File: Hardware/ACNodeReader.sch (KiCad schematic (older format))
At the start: 34 parts, among them J1 Conn_01x08_Male, J2 AVR-ISP-6, J3 Conn_01x04_Female, J4 Conn_01x02_Male, J5 Conn_01x04_Female, J6 Conn_01x04_Male, J7 Conn_01x04_Male, U1 L78L05_SOT89, U2 ATmega88PB-AU, U3 ISL8489EIBZ, U4 LM75C, Y1 Crystal_GND24

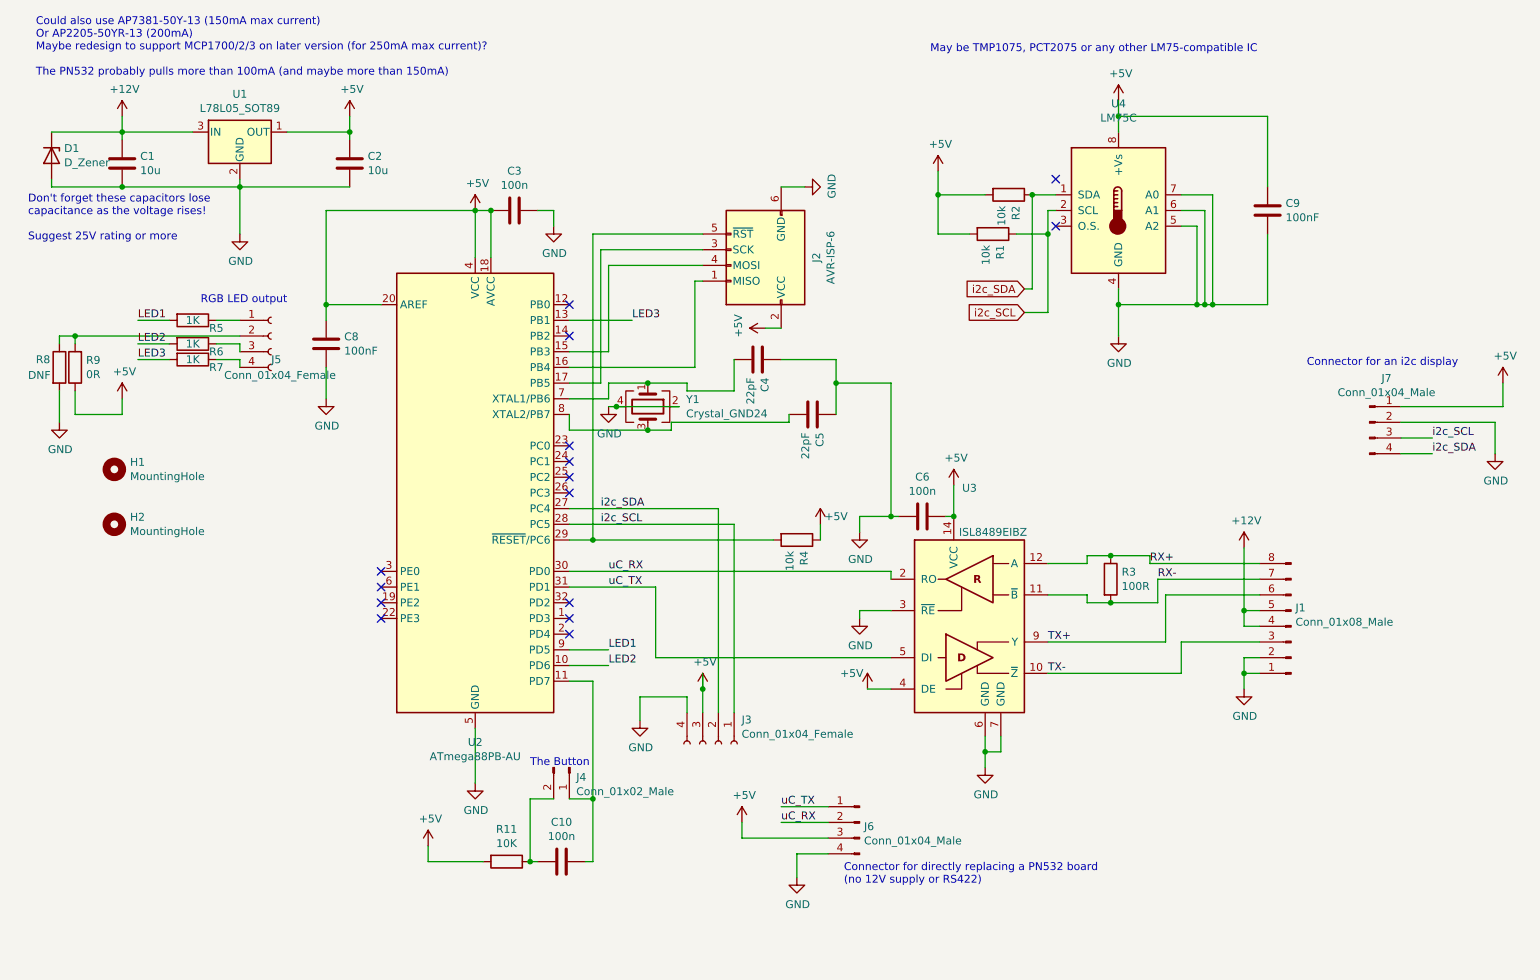
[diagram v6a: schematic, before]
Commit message: Hardware V1.1 - 3.3V with chunkier 5V regulator
The 1.0 5V regulator wasn't chunky enough, so this board has a larger
one to support the current draw of the PN532 module. Additionally, a
capacitor has been added near to the PN532 module connector to assist in
smoothing the supply to it.

Most of the board now runs at 3.3V, derived from the 5V rail. This is to
support direct connection to an ACNode, which only support 3.3V IO. This
required slowing the AVR down to 12MHz. An alternative option would have
been to use a level shifter on the TX line.
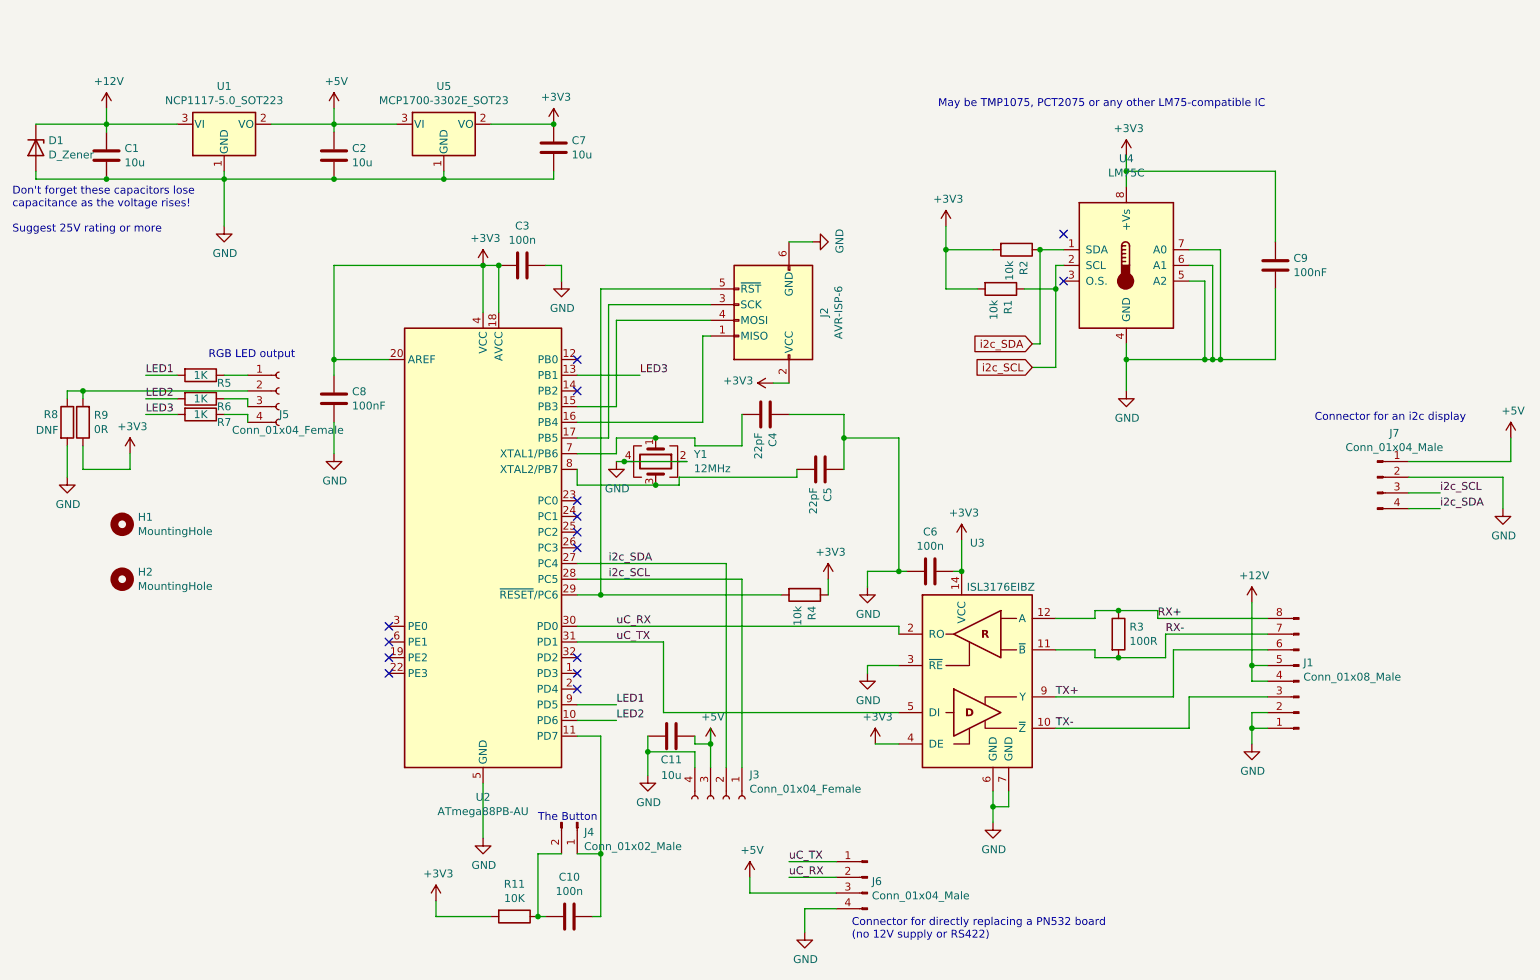
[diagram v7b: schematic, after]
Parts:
- removed U1: L78L05_SOT89, Package_TO_SOT_SMD:SOT-89-3, symbol Regulator_Linear:L78L05_SOT89
- added C11, C7: 10u, Capacitor_SMD:C_0805_2012Metric, symbol Device:C
- added U1: NCP1117-5.0_SOT223, Package_TO_SOT_SMD:SOT-223-3_TabPin2, symbol Regulator_Linear:NCP1117-5.0_SOT223
- added U5: MCP1700-3302E_SOT23, Package_TO_SOT_SMD:SOT-23, symbol Regulator_Linear:MCP1700-3302E_SOT23
- U3: value ISL8489EIBZ -> ISL3176EIBZ
- Y1: value Crystal_GND24 -> 12MHz
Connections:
- net +12V: now also U1.3 (VI)
- net +5V: now also C11.1, U1.2 (VO), U5.3 (VI); no longer C3.2, C6.1, C8.1, C9.1, J2.2 (VCC), R1.2, R11.2, R2.2, R4.1, R9.1, U2.18 (AVCC), U2.20 (AREF), U2.4 (VCC), U3.14 (VCC), U3.4 (DE), U4.8 (+Vs)
- net GND: now also C11.2, C7.2, U1.1 (GND), U5.1 (GND)
- new net +3V3: C3.2, C6.1, C7.1, C8.1, C9.1, J2.2 (VCC), R1.2, R11.2, R2.2, R4.1, R9.1, U2.18 (AVCC), U2.20 (AREF), U2.4 (VCC), U3.14 (VCC), U3.4 (DE), U4.8 (+Vs), U5.2 (VO)
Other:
- note removed: "Could also use AP7381-50Y-13 (150mA max current)\nOr AP2205-50YR-13 (200mA)\nMaybe redesign to support MCP1700/2/3 on later version (for 250mA max current)?\n\nThe PN532 probably pulls more than 100mA (and maybe more than 150mA)\n"
- moved on the sheet: C1, C10, C2, C3, C4, C5, C6, C8, C9, D1, H1, H2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

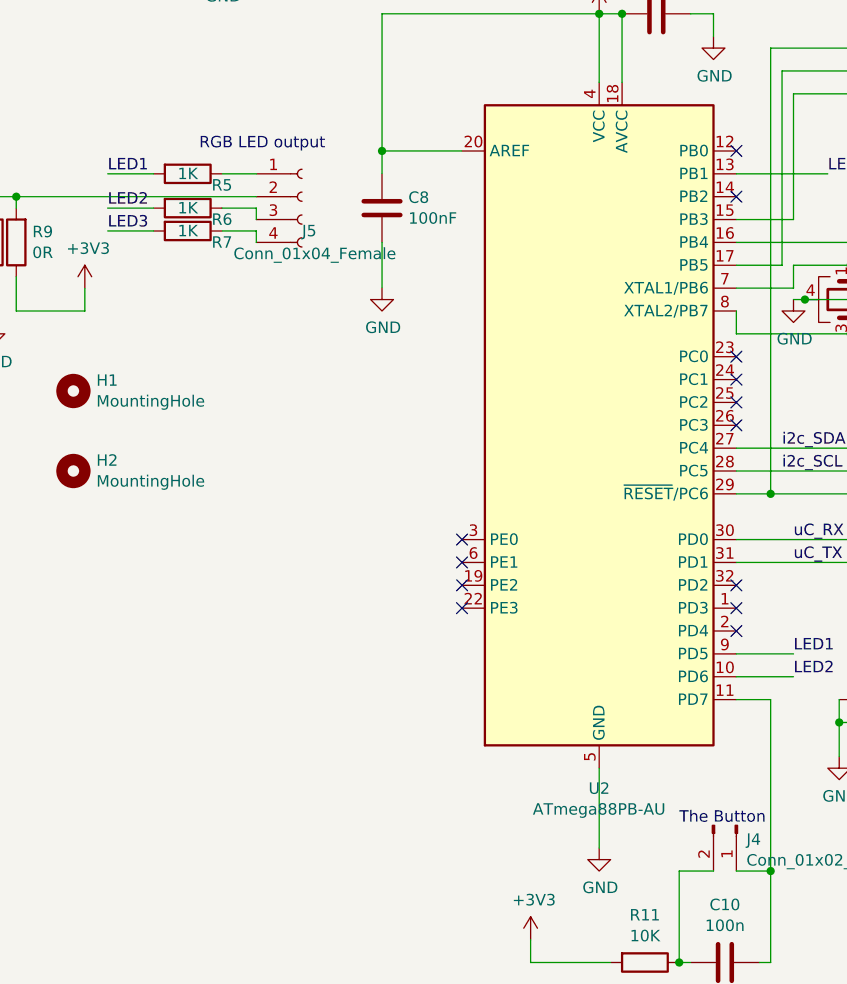
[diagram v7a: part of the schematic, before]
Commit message: Updated hardware with how I actually assembled it
I'm leaning towards the ATmega328PB, and also switched to 330R resistors on the LEDs
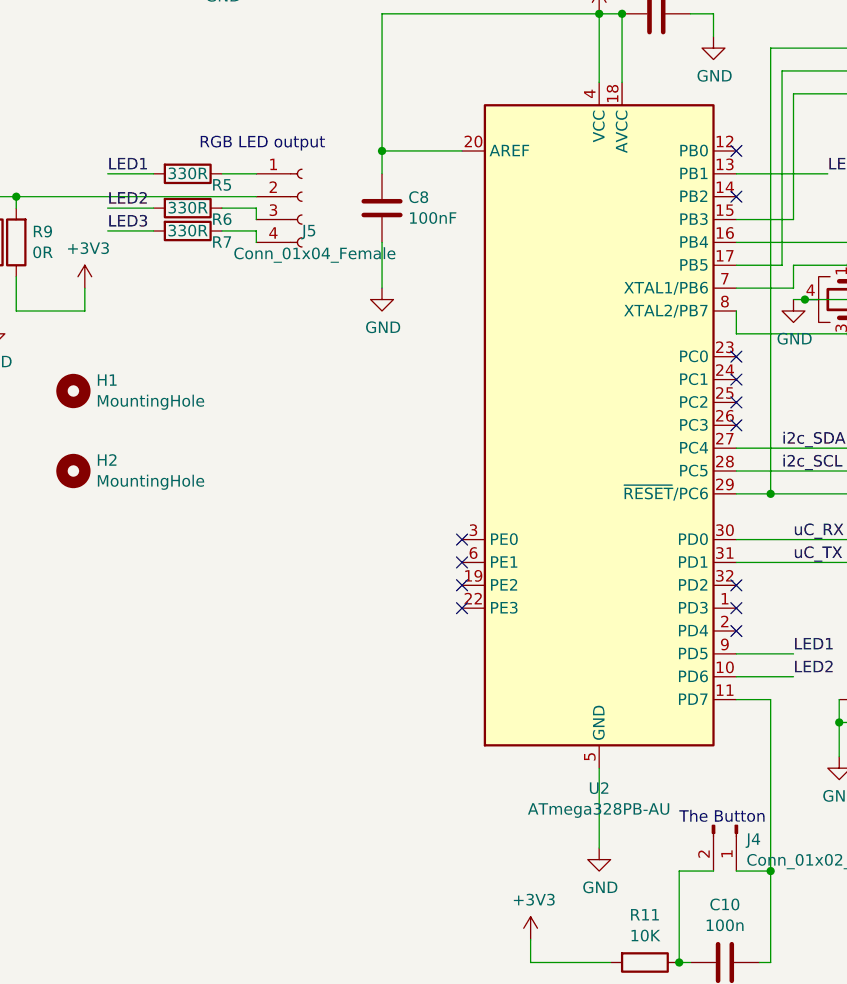
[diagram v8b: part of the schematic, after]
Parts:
- R5, R6, R7: value 1K -> 330R
- U2: value ATmega88PB-AU -> ATmega328PB-AU
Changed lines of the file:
@@
 P 1700 2900
 F 0 "R5" V 1750 3050 50  0000 C CNN
-F 1 "1K" V 1700 2900 50  0000 C CNN
+F 1 "330R" V 1700 2900 50  0000 C CNN
 F 2 "Resistor_SMD:R_0603_1608Metric" V 1630 2900 50  0001 C CNN
 F 3 "~" H 1700 2900 50  0001 C CNN
@@
 P 1700 3050
 F 0 "R6" V 1750 3200 50  0000 C CNN
-F 1 "1K" V 1700 3050 50  0000 C CNN
+F 1 "330R" V 1700 3050 50  0000 C CNN
 F 2 "Resistor_SMD:R_0603_1608Metric" V 1630 3050 50  0001 C CNN
 F 3 "~" H 1700 3050 50  0001 C CNN
@@
 P 1700 3150
 F 0 "R7" V 1750 3300 50  0000 C CNN
-F 1 "1K" V 1700 3150 50  0000 C CNN
+F 1 "330R" V 1700 3150 50  0000 C CNN
 F 2 "Resistor_SMD:R_0603_1608Metric" V 1630 3150 50  0001 C CNN
 F 3 "~" H 1700 3150 50  0001 C CNN
@@
 P 3500 4000
 F 0 "U2" H 3500 2411 50  0000 C CNN
-F 1 "ATmega88PB-AU" H 3500 2320 50  0000 C CNN
+F 1 "ATmega328PB-AU" H 3500 2320 50  0000 C CNN
 F 2 "Package_QFP:TQFP-32_7x7mm_P0.8mm" H 3500 4000 50  0001 C CIN
-F 3 "http://ww1.microchip.com/downloads/en/DeviceDoc/40001909A.pdf" H 3500 4000 50  0001 C CNN
+F 3 "http://ww1.microchip.com/downloads/en/DeviceDoc/40001906A.pdf" H 3500 4000 50  0001 C CNN
 	1    3500 4000
 	1    0    0    -1
